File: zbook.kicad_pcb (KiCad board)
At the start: 4 copper layers, 77 x 89 mm, 170 parts, among them J1 USB_C_Receptacle_USB2.0_16P, J2 USB_C_Receptacle_USB2.0_16P, J3 Conn_01x05_Pin, J4 Conn_01x05_Pin, J5 Conn_02x04_Odd_Even, J6 Conn_02x15_Counter_Clockwise, J7 MSD-4-A, J8 DISPLAY CONN, Q1 T2N7002AK,LM, Q2 FDN327N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

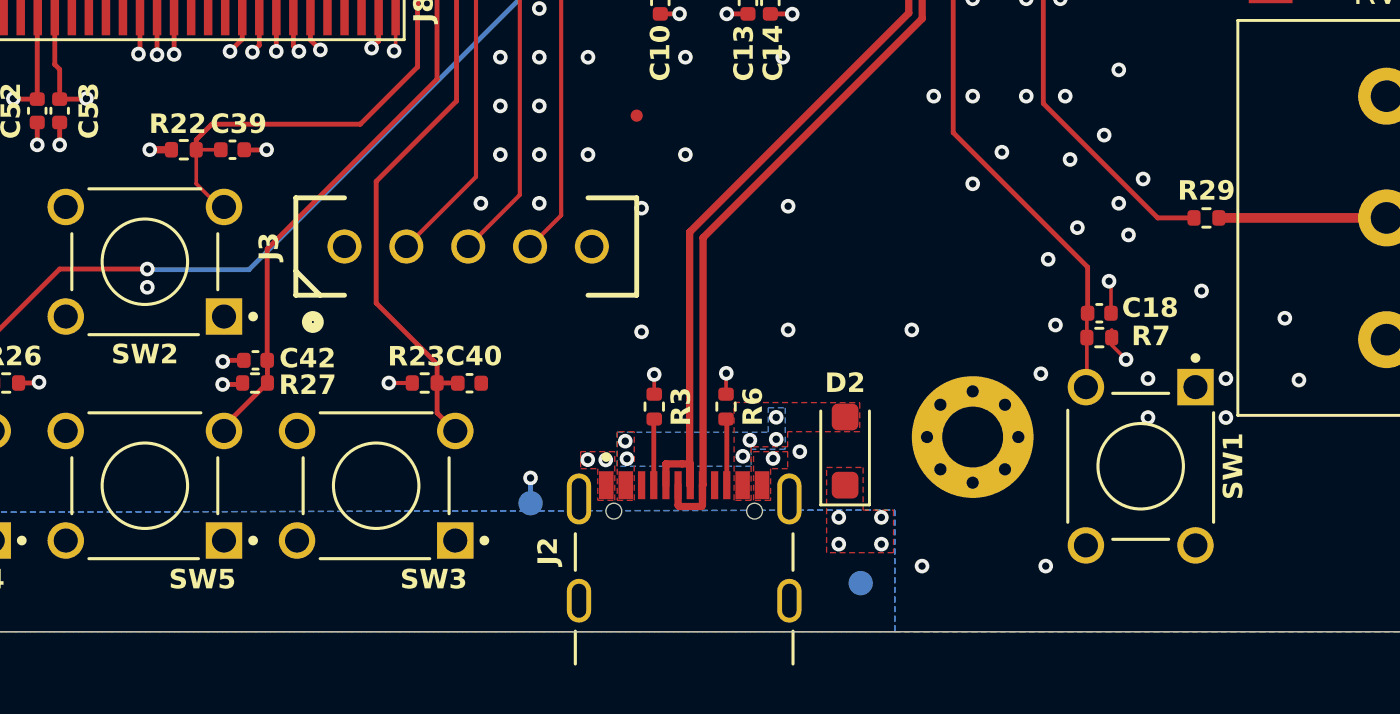
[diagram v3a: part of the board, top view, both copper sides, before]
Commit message: refac: aligns all buttons
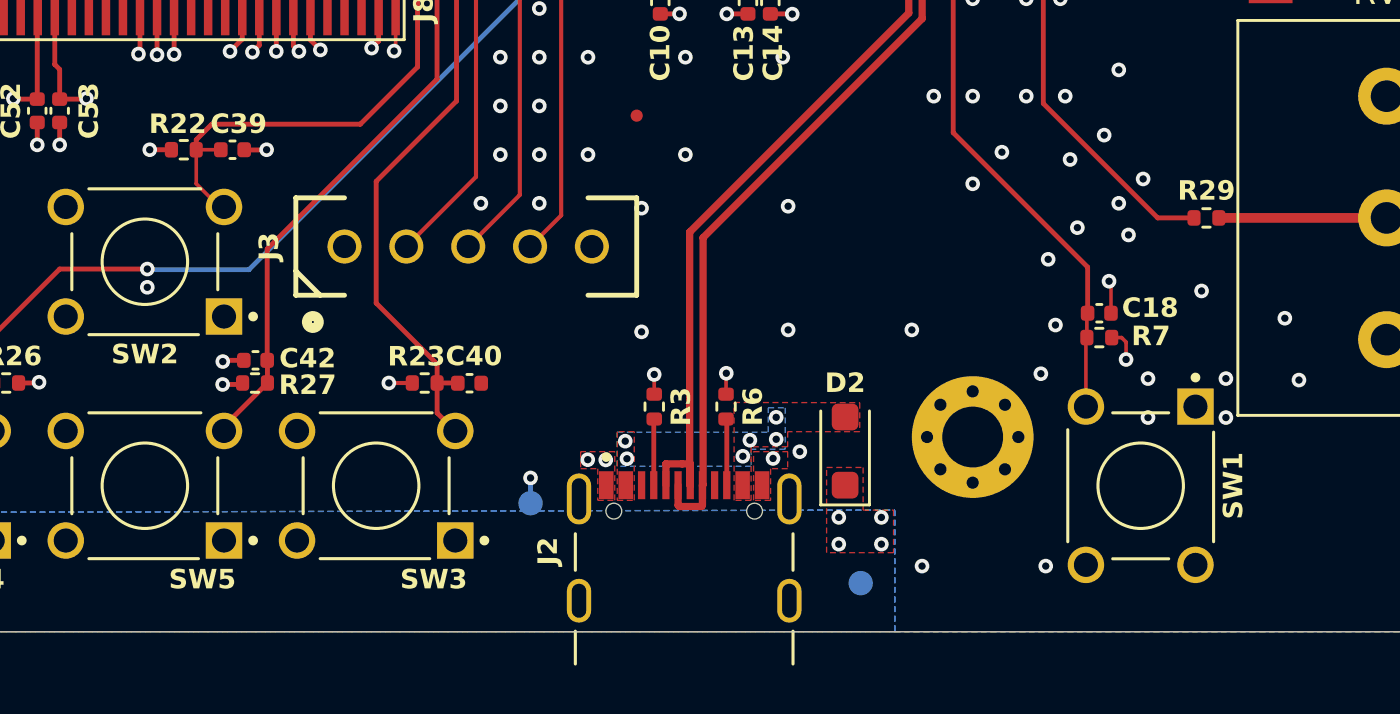
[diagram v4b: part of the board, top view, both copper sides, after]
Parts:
- moved SW1 0.80 mm to (163.9, 147.0)
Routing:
- net /Microcontroller/RUN_RP2350: track 58.3 -> 58.9 mm
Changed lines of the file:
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@@
 	(footprint "peripherals1:SW_1825910-6-4"
 		(layer "F.Cu")
-		(at 163.9 146.2 -90)
+		(at 163.9 147 -90)
 		(property "Reference" "SW1"
-			(at 0 -3.8 270)
+			(at 0 -3.8 90)
 			(layer "F.SilkS")
 			(effects
@@
 		)
 		(property "Value" "SW_Push"
-			(at 1.150079 3.960282 270)
+			(at 1.150079 3.960282 90)
 			(layer "F.Fab")
 			(effects
@@
 		)
 		(property "Datasheet" "https://www.digikey.com/en/products/detail/te-connectivity-alcoswitch-switches/1825910-6/1632536"
-			(at 0 0 270)
+			(at 0 0 90)
 			(layer "F.Fab")
 			(hide yes)
@@
 		)
 		(property "Description" "Push button switch, generic, two pins"
-			(at 0 0 270)
+			(at 0 0 90)
 			(layer "F.Fab")
 			(hide yes)
@@
 	)
 	(segment
-		(start 162.71 140.91)
-		(end 162.71 140.6)
-		(width 0.15)
-		(layer "F.Cu")
-		(net 4)
-	)
-	(segment
 		(start 152.82 91.78)
 		(end 152.8 91.8)
@@
 	)
 	(segment
+		(start 163.3 141.1)
+		(end 163.115 140.915)
+		(width 0.15)
+		(layer "F.Cu")
+		(net 4)
+	)
+	(segment
 		(start 138.24 101.74)
 		(end 138.3 101.8)
@@
 	)
 	(segment
+		(start 163.115 140.915)
+		(end 162.71 140.915)
+		(width 0.15)
+		(layer "F.Cu")
+		(net 4)
+	)
+	(segment
 		(start 144.17 116.66)
 		(end 143.34 116.66)
@@
 		(start 124.09 133.2)
 		(end 123.2 133.2)
-		(width 0.3)
+		(width 0.2)
 		(layer "F.Cu")
 		(net 4)
@@
 	)
 	(segment
+		(start 163.3 141.815)
+		(end 163.3 141.1)
+		(width 0.15)
+		(layer "F.Cu")
+		(net 4)
+	)
+	(segment
 		(start 144.3 101.9)
 		(end 144.3 102.1)
@@
 	)
 	(segment
-		(start 163.3 141.815)
-		(end 162.71 141.225)
-		(width 0.15)
-		(layer "F.Cu")
-		(net 4)
-	)
-	(segment
 		(start 113.5 89.5)
 		(end 113.5 86.83)
@@
 	)
 	(segment
+		(start 161.65 141.13)
+		(end 161.65 143.75)
+		(width 0.15)
+		(layer "F.Cu")
+		(net 8)
+	)
+	(segment
 		(start 155.1 110.029229)
 		(end 155.1 116.3)
@@
 	)
 	(segment
-		(start 161.69 140.915)
-		(end 161.69 143.005)
-		(width 0.15)
+		(start 156.2 121.4)
+		(end 156.2 132.5)
+		(width 0.2)
 		(layer "F.Cu")
 		(net 8)
 	)
 	(segment
-		(start 161.69 143.005)
-		(end 161.75 143.065)
+		(start 161.69 141.09)
+		(end 161.65 141.13)
 		(width 0.15)
 		(layer "F.Cu")
@@
 	)
 	(segment
-		(start 156.2 121.4)
-		(end 156.2 132.5)
-		(width 0.2)
+		(start 161.69 140.915)
+		(end 161.69 141.09)
+		(width 0.15)
 		(layer "F.Cu")
 		(net 8)
